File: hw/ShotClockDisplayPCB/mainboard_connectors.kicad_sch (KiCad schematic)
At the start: 0 parts

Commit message: Started on second PCB, and added 5V regulator
5V regulator added to main pcb for the segment displays, using same TPS63000 chip, but with a different selector resistor to choose for 5V

Added second project to contain the display PCBA design.

Calculated the current usage of the displays with different current limiting resistors on the LEDs.

Calculated the  current limit resistors for transistors behind LEDs
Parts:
- added J1: PH-00041, PH-00041:HDR-TH_20P-P2.54-V-M-R2-C10-S2.54, symbol PH-00041_corr:PH-00041
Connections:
- new net +5V: J1.1
- new net DISP1_SEG_A: J1.2
- new net DISP1_SEG_B: J1.3
- new net DISP1_SEG_C: J1.4
- new net DISP1_SEG_D: J1.5
- new net DISP1_SEG_DP: J1.9
- new net DISP1_SEG_E: J1.6
- new net DISP1_SEG_F: J1.7
- new net DISP1_SEG_G: J1.8
- new net DISP2_SEG_A: J1.10
- new net DISP2_SEG_B: J1.11
- new net DISP2_SEG_C: J1.12
- new net DISP2_SEG_D: J1.13
- new net DISP2_SEG_DP: J1.17
- new net DISP2_SEG_E: J1.14
- new net DISP2_SEG_F: J1.15
- new net DISP2_SEG_G: J1.16
- new net GND: J1.19
- new net TIM2_CH1_PWM1_SEG: J1.18
- new net TIM2_CH2_PWM2_SEG: J1.20
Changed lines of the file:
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@@
 (kicad_sch (version 20230121) (generator eeschema)
   (paper "A4")
+  (wire (pts (xy 64.77 66.04) (xy 44.45 66.04))
+    (stroke (width 0) (type default))
+  )
+  (wire (pts (xy 44.45 66.04) (xy 44.45 67.31))
+    (stroke (width 0) (type default))
+  )
+  (wire (pts (xy 44.45 43.18) (xy 44.45 41.91))
+    (stroke (width 0) (type default))
+  )
+  (wire (pts (xy 44.45 43.18) (xy 64.77 43.18))
+    (stroke (width 0) (type default))
+  )
+  (hierarchical_label "TIM2_CH1_PWM1_SEG" (shape output) (at 80.01 63.5 0) (fields_autoplaced)
+    (effects (font (size 1.27 1.27)) (justify left))
+  )
+  (hierarchical_label "DISP1_SEG_G" (shape output) (at 80.01 50.8 0) (fields_autoplaced)
+    (effects (font (size 1.27 1.27)) (justify left))
+  )
+  (hierarchical_label "DISP1_SEG_DP" (shape output) (at 64.77 53.34 180) (fields_autoplaced)
+    (effects (font (size 1.27 1.27)) (justify right))
+  )
+  (hierarchical_label "DISP2_SEG_D" (shape output) (at 64.77 58.42 180) (fields_autoplaced)
+    (effects (font (size 1.27 1.27)) (justify right))
+  )
+  (hierarchical_label "DISP1_SEG_B" (shape output) (at 64.77 45.72 180) (fields_autoplaced)
+    (effects (font (size 1.27 1.27)) (justify right))
+  )
+  (hierarchical_label "DISP2_SEG_A" (shape output) (at 80.01 53.34 0) (fields_autoplaced)
+    (effects (font (size 1.27 1.27)) (justify left))
+  )
+  (hierarchical_label "DISP2_SEG_B" (shape output) (at 64.77 55.88 180) (fields_autoplaced)
+    (effects (font (size 1.27 1.27)) (justify right))
+  )
+  (hierarchical_label "DISP2_SEG_DP" (shape output) (at 64.77 63.5 180) (fields_autoplaced)
+    (effects (font (size 1.27 1.27)) (justify right))
+  )
+  (hierarchical_label "DISP1_SEG_C" (shape output) (at 80.01 45.72 0) (fields_autoplaced)
+    (effects (font (size 1.27 1.27)) (justify left))
+  )
+  (hierarchical_label "DISP2_SEG_F" (shape output) (at 64.77 60.96 180) (fields_autoplaced)
+    (effects (font (size 1.27 1.27)) (justify right))
+  )
+  (hierarchical_label "DISP2_SEG_G" (shape output) (at 80.01 60.96 0) (fields_autoplaced)
+    (effects (font (size 1.27 1.27)) (justify left))
+  )
+  (hierarchical_label "DISP1_SEG_A" (shape output) (at 80.01 43.18 0) (fields_autoplaced)
+    (effects (font (size 1.27 1.27)) (justify left))
+  )
+  (hierarchical_label "DISP1_SEG_F" (shape output) (at 64.77 50.8 180) (fields_autoplaced)
+    (effects (font (size 1.27 1.27)) (justify right))
+  )
+  (hierarchical_label "DISP2_SEG_C" (shape output) (at 80.01 55.88 0) (fields_autoplaced)
+    (effects (font (size 1.27 1.27)) (justify left))
+  )
+  (hierarchical_label "DISP1_SEG_E" (shape output) (at 80.01 48.26 0) (fields_autoplaced)
+    (effects (font (size 1.27 1.27)) (justify left))
+  )
+  (hierarchical_label "DISP1_SEG_D" (shape output) (at 64.77 48.26 180) (fields_autoplaced)
+    (effects (font (size 1.27 1.27)) (justify right))
+  )
+  (hierarchical_label "DISP2_SEG_E" (shape output) (at 80.01 58.42 0) (fields_autoplaced)
+    (effects (font (size 1.27 1.27)) (justify left))
+  )
+  (hierarchical_label "TIM2_CH2_PWM2_SEG" (shape output) (at 80.01 66.04 0) (fields_autoplaced)
+    (effects (font (size 1.27 1.27)) (justify left))
+  )
+  (symbol (lib_id "power:GND") (at 44.45 67.31 0) (unit 1)
+    (in_bom yes) (on_board yes) (dnp no) (fields_autoplaced)
+    (property "Reference" "#PWR026" (at 44.45 73.66 0)
+      (effects (font (size 1.27 1.27)) hide)
+    )
+    (property "Value" "GND" (at 44.45 72.39 0)
+      (effects (font (size 1.27 1.27)) hide)
+    )
+    (property "Footprint" "" (at 44.45 67.31 0)
+      (effects (font (size 1.27 1.27)) hide)
+    )
+    (property "Datasheet" "" (at 44.45 67.31 0)
+      (effects (font (size 1.27 1.27)) hide)
+    )
+    (pin "1")
+    (instances
+      (project "ShotClockProject"
+        (path "/5fd859aa-754d-49c2-9762-3f7ebe3bb64c"
+          (reference "#PWR026") (unit 1)
+        )
+        (path "/5fd859aa-754d-49c2-9762-3f7ebe3bb64c/d287d155-1951-4d4f-8d6c-570f03bc79f5"
+          (reference "#PWR023") (unit 1)
+        )
+        (path "/5fd859aa-754d-49c2-9762-3f7ebe3bb64c/dbe9281d-d28a-4966-832c-4ef9ca7a9777"
+          (reference "#PWR062") (unit 1)
+        )
+      )
+      (project "ShotClockDisplayPCB"
+        (path "/baf3f1b3-1588-4756-b7d1-50b7c58bafb0/acc83e16-b7da-48bd-ac1b-341a95513ee6"
+          (reference "#PWR02") (unit 1)
+        )
+      )
+    )
+  )
+  (symbol (lib_id "power:+5V") (at 44.45 41.91 0) (unit 1)
+    (in_bom yes) (on_board yes) (dnp no) (fields_autoplaced)
+    (property "Reference" "#PWR01" (at 44.45 45.72 0)
+      (effects (font (size 1.27 1.27)) hide)
+    )
+    (property "Value" "+5V" (at 44.45 36.83 0)
+      (effects (font (size 1.27 1.27)))
+    )
+    (property "Footprint" "" (at 44.45 41.91 0)
+      (effects (font (size 1.27 1.27)) hide)
+    )
+    (property "Datasheet" "" (at 44.45 41.91 0)
+      (effects (font (size 1.27 1.27)) hide)
+    )
+    (pin "1")
+    (instances
+      (project "ShotClockDisplayPCB"
+        (path "/baf3f1b3-1588-4756-b7d1-50b7c58bafb0/acc83e16-b7da-48bd-ac1b-341a95513ee6"
+          (reference "#PWR01") (unit 1)
+        )
+      )
+    )
+  )
+  (symbol (lib_id "PH-00041_corr:PH-00041") (at 72.39 54.61 0) (unit 1)
+    (in_bom yes) (on_board yes) (dnp no) (fields_autoplaced)
+    (property "Reference" "J1" (at 72.39 35.56 0)
+      (effects (font (size 1.27 1.27)))
+    )
+    (property "Value" "PH-00041" (at 72.39 38.1 0)
+      (effects (font (size 1.27 1.27)))
+    )
+    (property "Footprint" "PH-00041:HDR-TH_20P-P2.54-V-M-R2-C10-S2.54" (at 72.39 73.66 0)
+      (effects (font (size 1.27 1.27)) hide)
+    )
+    (property "Datasheet" "" (at 72.39 54.61 0)
+      (effects (font (size 1.27 1.27)) hide)
+    )
+    (property "Manufacturer" "Liansheng(连盛)" (at 72.39 76.2 0)
+      (effects (font (size 1.27 1.27)) hide)
+    )
+    (property "LCSC Part" "C2830008" (at 72.39 78.74 0)
+      (effects (font (size 1.27 1.27)) hide)
+    )
+    (pin "1")
+    (pin "10")
+    (pin "11")
+    (pin "12")
+    (pin "13")
+    (pin "14")
+    (pin "15")
+    (pin "16")
+    (pin "17")
+    (pin "18")
+    (pin "19")
+    (pin "2")
+    (pin "20")
+    (pin "3")
+    (pin "4")
+    (pin "5")
+    (pin "6")
+    (pin "7")
+    (pin "8")
+    (pin "9")
+    (instances
+      (project "ShotClockDisplayPCB"
+        (path "/baf3f1b3-1588-4756-b7d1-50b7c58bafb0/acc83e16-b7da-48bd-ac1b-341a95513ee6"
+          (reference "J1") (unit 1)
+        )
+      )
+    )
+  )
 )

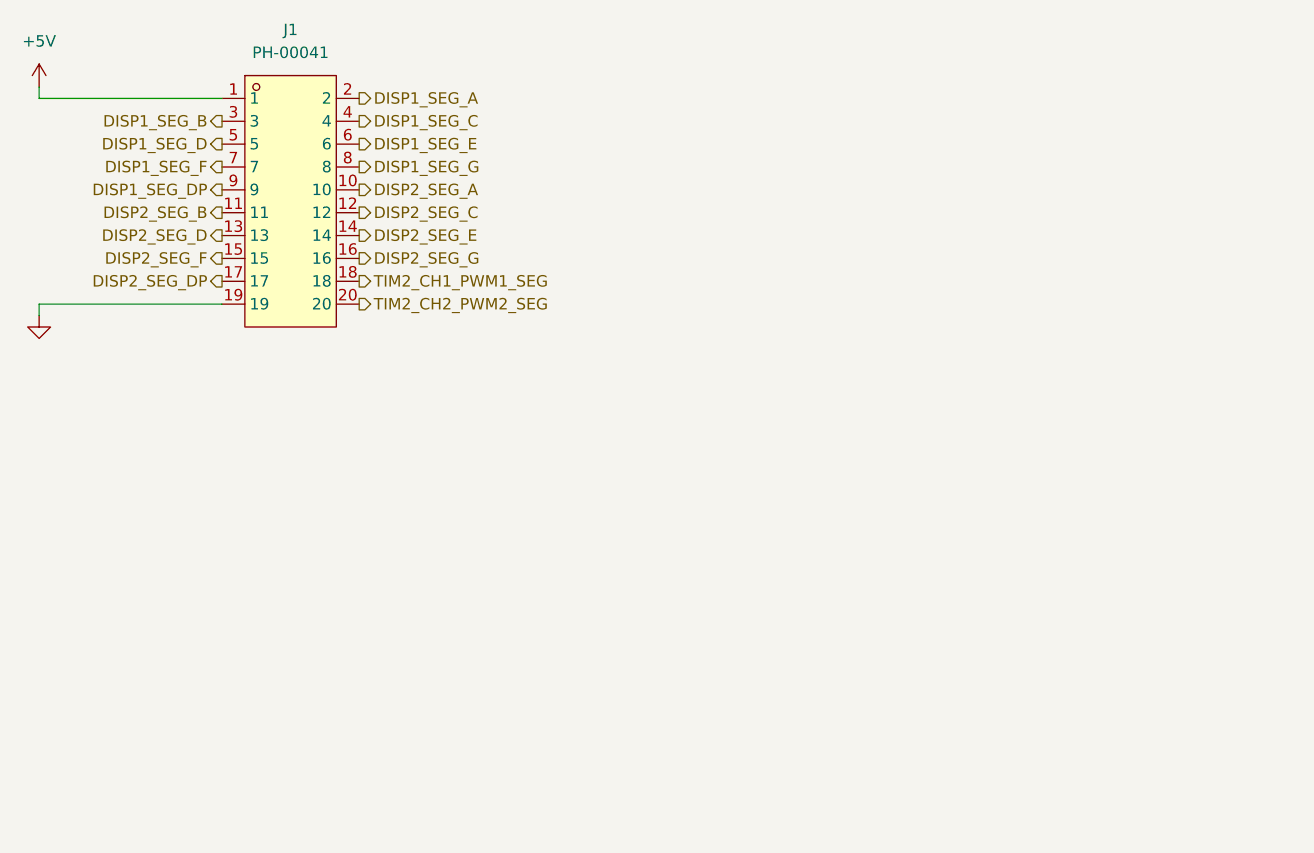
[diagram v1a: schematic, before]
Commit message: Display print
Changed mainboard connector to FPC connector
Created routing for board
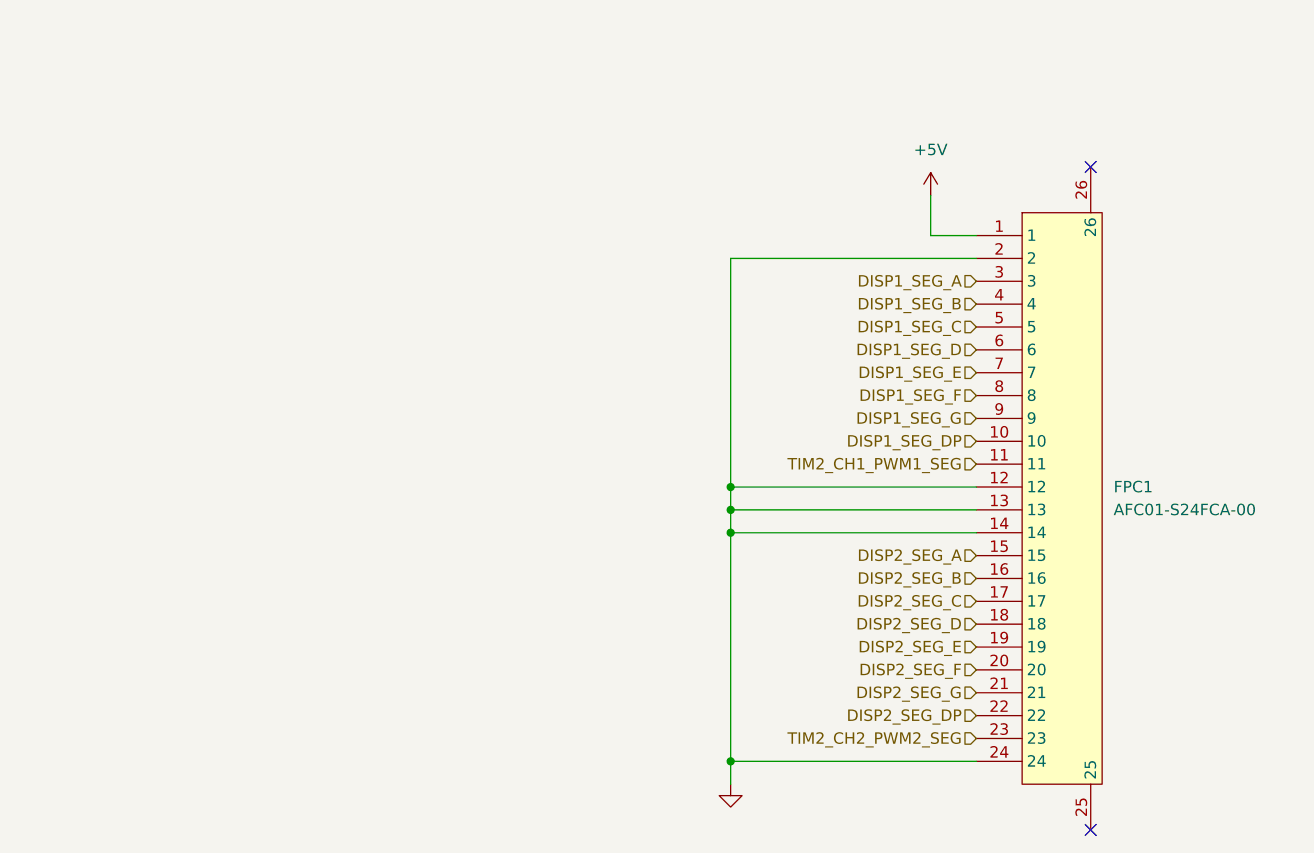
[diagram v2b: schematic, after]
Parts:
- removed J1: PH-00041, PH-00041:HDR-TH_20P-P2.54-V-M-R2-C10-S2.54, symbol PH-00041_corr:PH-00041
- added FPC1: AFC01-S24FCA-00, AFC01-S24FCA-00:FPC-SMD_P0.50-24P_FGS-XJ-H2.0, symbol AFC01-S24FCA-00:AFC01-S24FCA-00
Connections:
- net +5V: now also FPC1.1
- net DISP1_SEG_A: now also FPC1.3
- net DISP1_SEG_B: now also FPC1.4
- net DISP1_SEG_C: now also FPC1.5
- net DISP1_SEG_D: now also FPC1.6
- net DISP1_SEG_DP: now also FPC1.10
- net DISP1_SEG_E: now also FPC1.7
- net DISP1_SEG_F: now also FPC1.8
- net DISP1_SEG_G: now also FPC1.9
- net DISP2_SEG_A: now also FPC1.15
- net DISP2_SEG_B: now also FPC1.16
- net DISP2_SEG_C: now also FPC1.17
- net DISP2_SEG_D: now also FPC1.18
- net DISP2_SEG_DP: now also FPC1.22
- net DISP2_SEG_E: now also FPC1.19
- net DISP2_SEG_F: now also FPC1.20
- net DISP2_SEG_G: now also FPC1.21
- net GND: now also FPC1.12, FPC1.13, FPC1.14, FPC1.2, FPC1.24
- net TIM2_CH1_PWM1_SEG: now also FPC1.11
- net TIM2_CH2_PWM2_SEG: now also FPC1.23
- no-connect marks 0 -> 2

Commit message: Cleaned second print
and added new connectors, pinout and removed all REV1 stuff.
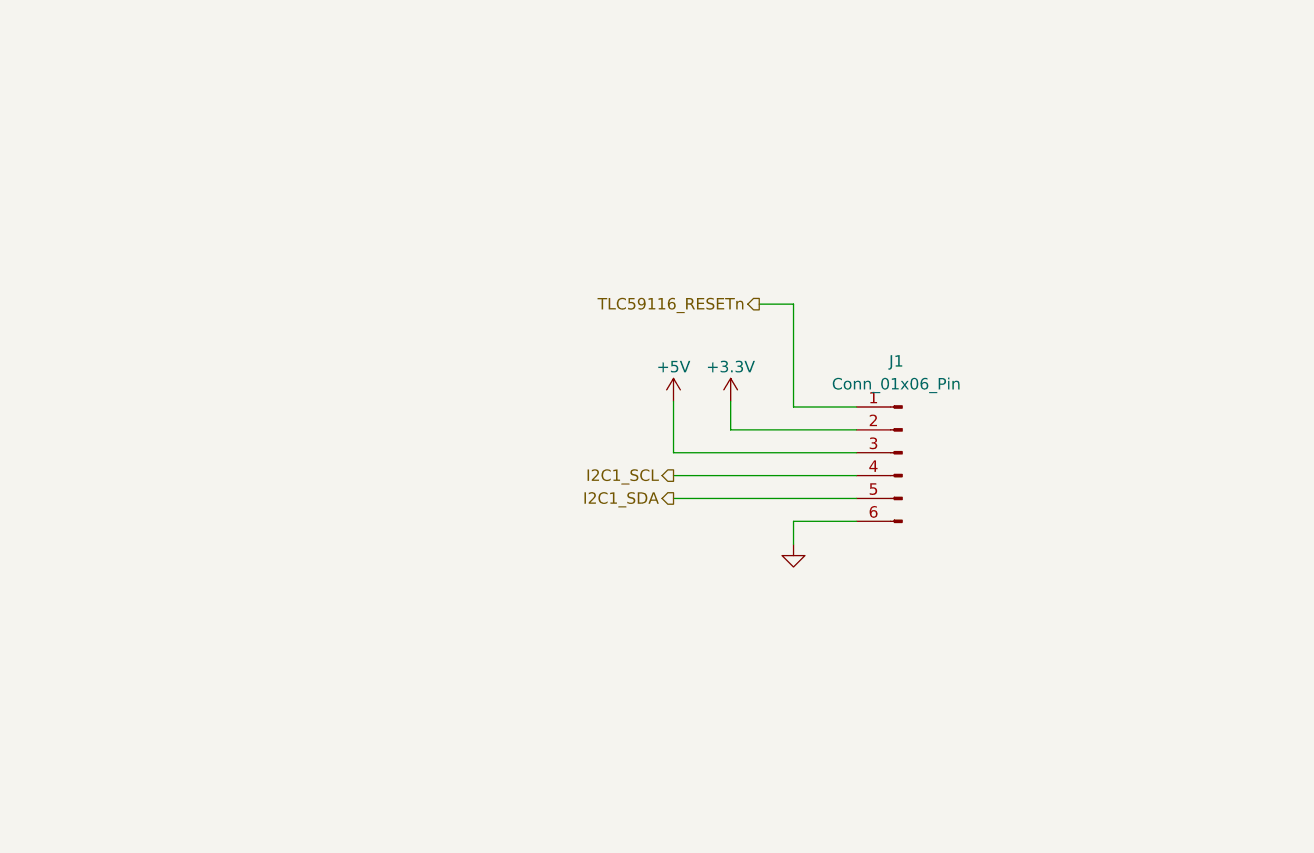
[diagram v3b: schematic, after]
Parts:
- removed FPC1: AFC01-S24FCA-00, AFC01-S24FCA-00:FPC-SMD_P0.50-24P_FGS-XJ-H2.0, symbol AFC01-S24FCA-00:AFC01-S24FCA-00
- added J1: Conn_01x06_Pin, Connector_PinHeader_2.54mm:PinHeader_1x06_P2.54mm_Vertical, symbol Connector:Conn_01x06_Pin
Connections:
- net +5V: now also J1.3 (Pin_3)
- net GND: now also J1.6 (Pin_6)
- new net +3.3V: J1.2 (Pin_2)
- new net I2C1_SCL: J1.4 (Pin_4)
- new net I2C1_SDA: J1.5 (Pin_5)
- new net TLC59116_RESETn: J1.1 (Pin_1)
- no-connect marks 2 -> 0

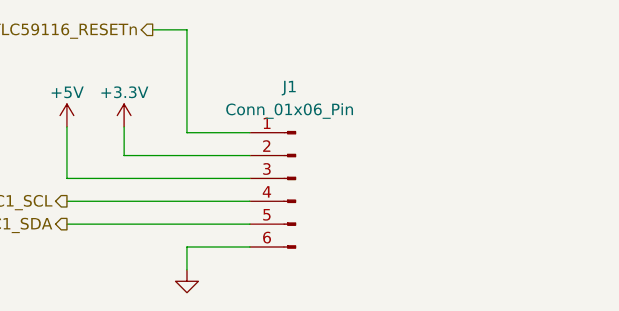
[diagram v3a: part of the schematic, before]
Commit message: Changed display connectors to JST PH 2.0mm
In docs, schematic and footprints
Both sides, connect with male/male cable
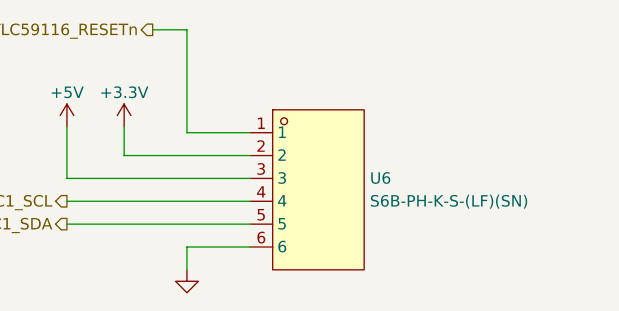
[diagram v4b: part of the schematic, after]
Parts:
- removed J1: Conn_01x06_Pin, Connector_PinHeader_2.54mm:PinHeader_1x06_P2.54mm_Vertical, symbol Connector:Conn_01x06_Pin
- added U6: S6B-PH-K-S-(LF)(SN), S6B_PH_K_S_LF_SN:CONN-TH_6P-P2.00_S6B-PH-K-S-LF-SN, symbol S6B_PH_K_S_LF_SN:S6B-PH-K-S-(LF)(SN)
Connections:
- net +3.3V: now also U6.2
- net +5V: now also U6.3
- net GND: now also U6.6
- net I2C1_SCL: now also U6.4
- net I2C1_SDA: now also U6.5
- net TLC59116_RESETn: now also U6.1
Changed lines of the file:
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@@
     )
   )
-  (symbol (lib_id "Connector:Conn_01x06_Pin") (at 140.335 82.55 0) (mirror y) (unit 1)
-    (in_bom yes) (on_board yes) (dnp no)
-    (property "Reference" "J1" (at 139.7 72.39 0)
-      (effects (font (size 1.27 1.27)))
+  (symbol (lib_id "S6B_PH_K_S_LF_SN:S6B-PH-K-S-(LF)(SN)") (at 140.335 85.09 0) (unit 1)
+    (in_bom yes) (on_board yes) (dnp no) (fields_autoplaced)
+    (property "Reference" "U6" (at 148.59 82.55 0)
+      (effects (font (size 1.27 1.27)) (justify left))
     )
-    (property "Value" "Conn_01x06_Pin" (at 139.7 74.93 0)
-      (effects (font (size 1.27 1.27)))
+    (property "Value" "S6B-PH-K-S-(LF)(SN)" (at 148.59 85.09 0)
+      (effects (font (size 1.27 1.27)) (justify left))
     )
-    (property "Footprint" "Connector_PinHeader_2.54mm:PinHeader_1x06_P2.54mm_Vertical" (at 140.335 82.55 0)
+    (property "Footprint" "S6B_PH_K_S_LF_SN:CONN-TH_6P-P2.00_S6B-PH-K-S-LF-SN" (at 140.335 97.79 0)
       (effects (font (size 1.27 1.27)) hide)
     )
-    (property "Datasheet" "~" (at 140.335 82.55 0)
+    (property "Datasheet" "https://lcsc.com/product-detail/PH-Connectors_JST_S6B-PH-K-S-LF-SN_PHsocket-1-6P-Curved-needle-pitch2mm_C157920.html" (at 140.335 100.33 0)
       (effects (font (size 1.27 1.27)) hide)
     )
-    (property "LCSC Part #" "C37208" (at 140.335 82.55 0)
-      (effects (font (size 1.27 1.27)) hide)
-    )
-    (property "LCSC Part" "C37208" (at 140.335 82.55 0)
+    (property "LCSC Part" "C157920" (at 140.335 102.87 0)
       (effects (font (size 1.27 1.27)) hide)
     )
@@
     (instances
       (project "ShotClockProject"
-        (path "/5fd859aa-754d-49c2-9762-3f7ebe3bb64c/5bec211e-466d-46c6-9543-84cb75088ef1"
-          (reference "J1") (unit 1)
-        )
         (path "/5fd859aa-754d-49c2-9762-3f7ebe3bb64c/dbe9281d-d28a-4966-832c-4ef9ca7a9777"
-          (reference "J6") (unit 1)
+          (reference "U6") (unit 1)
         )
       )
       (project "ShotClockDisplayPCB"
         (path "/baf3f1b3-1588-4756-b7d1-50b7c58bafb0/acc83e16-b7da-48bd-ac1b-341a95513ee6"
-          (reference "J5") (unit 1)
+          (reference "U1") (unit 1)
         )
       )
